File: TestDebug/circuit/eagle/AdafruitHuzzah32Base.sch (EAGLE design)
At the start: 5 parts, among them J1 CORTEX_DEBUG_PTH

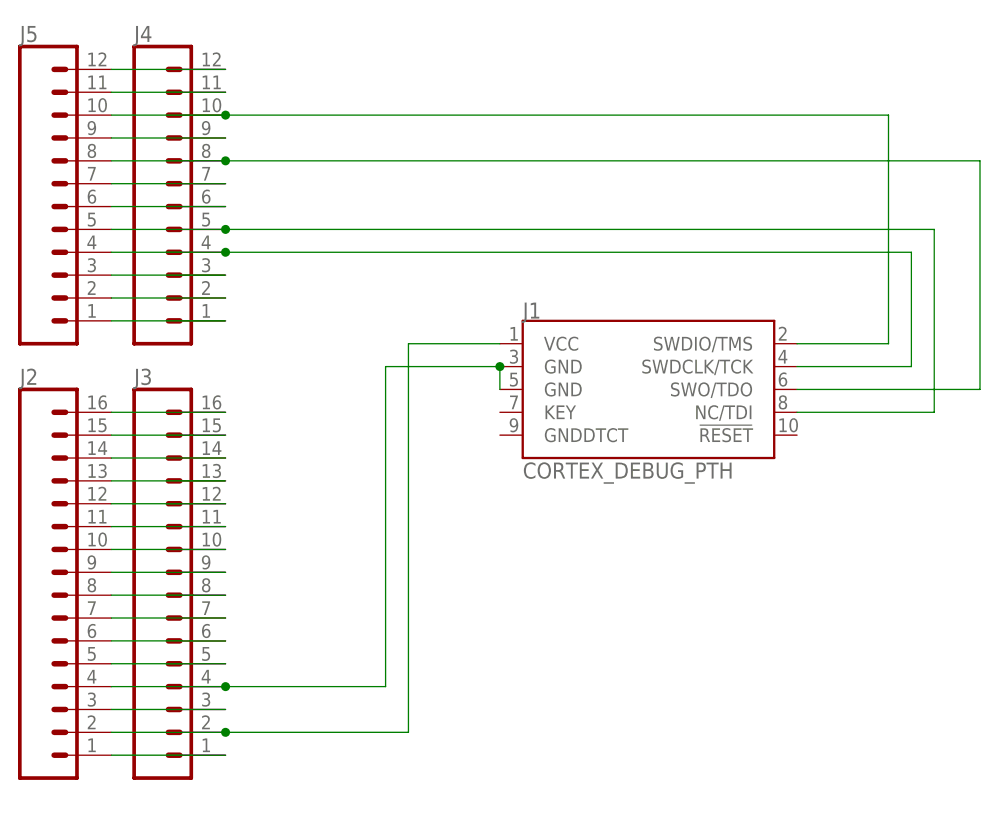
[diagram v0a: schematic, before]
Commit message: Added power pins and more silk screen
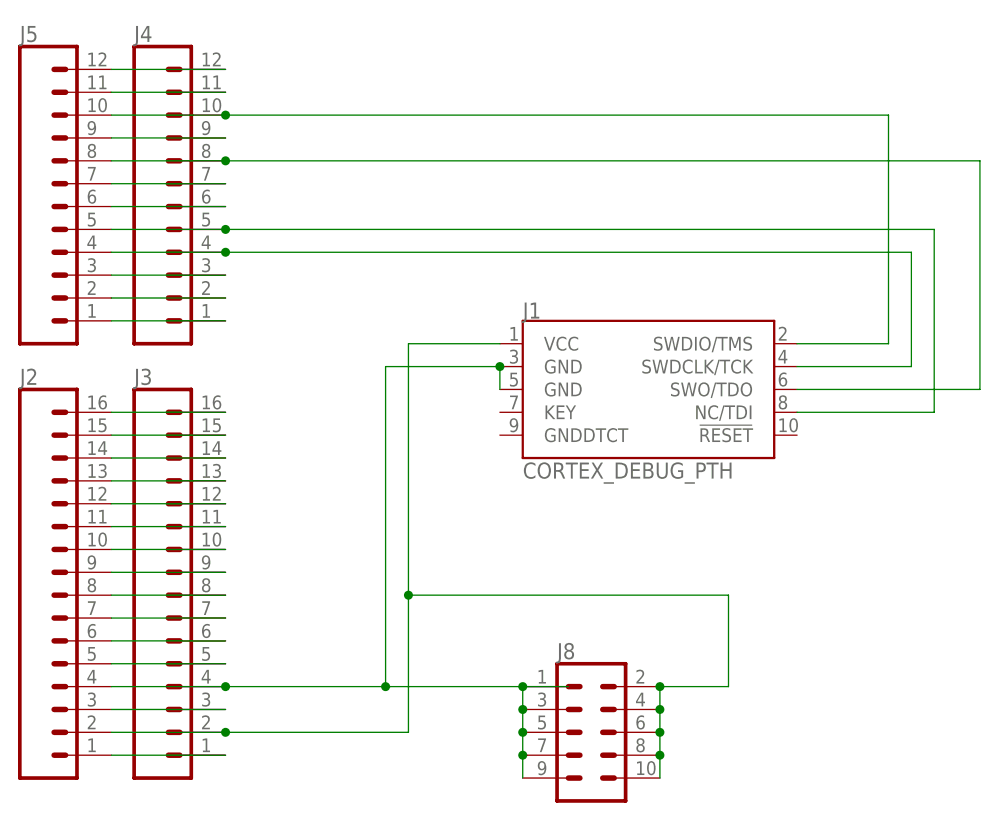
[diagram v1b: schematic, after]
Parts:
- added J8: (no value), SparkFun-Connectors:CONN_05X2PTH
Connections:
- net N$1: now also J8.10, J8.2, J8.4, J8.6, J8.8
- net N$2: now also J8.1, J8.3, J8.5, J8.7, J8.9
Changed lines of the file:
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@@
 <part name="J2" library="SparkFun-Connectors" library_urn="urn:adsk.eagle:library:513" deviceset="CONN_16" device="" package3d_urn="urn:adsk.eagle:package:38258/1"/>
 <part name="J5" library="SparkFun-Connectors" library_urn="urn:adsk.eagle:library:513" deviceset="CONN_12" device="" package3d_urn="urn:adsk.eagle:package:38169/1"/>
+<part name="J8" library="SparkFun-Connectors" library_urn="urn:adsk.eagle:library:513" deviceset="CONN_05X2" device="PTH" package3d_urn="urn:adsk.eagle:package:38012/1"/>
 </parts>
 <sheets>
@@
 <attribute name="NAME" x="50.8" y="104.648" size="1.778" layer="95" font="vector"/>
 </instance>
+<instance part="J8" gate="G$1" x="114.3" y="27.94" smashed="yes">
+<attribute name="VALUE" x="110.49" y="18.034" size="1.778" layer="96" font="vector"/>
+<attribute name="NAME" x="110.49" y="36.068" size="1.778" layer="95" font="vector"/>
+</instance>
 </instances>
 <busses>
@@
 <pinref part="J3" gate="G$1" pin="2"/>
 <wire x1="73.66" y1="27.94" x2="93.98" y2="27.94" width="0.1524" layer="91"/>
-<wire x1="93.98" y1="27.94" x2="93.98" y2="71.12" width="0.1524" layer="91"/>
+<wire x1="93.98" y1="27.94" x2="93.98" y2="43.18" width="0.1524" layer="91"/>
 <pinref part="J1" gate="G$1" pin="VCC"/>
+<wire x1="93.98" y1="43.18" x2="93.98" y2="71.12" width="0.1524" layer="91"/>
 <wire x1="93.98" y1="71.12" x2="104.14" y2="71.12" width="0.1524" layer="91"/>
 <pinref part="J2" gate="G$1" pin="2"/>
 <wire x1="60.96" y1="27.94" x2="73.66" y2="27.94" width="0.1524" layer="91"/>
 <junction x="73.66" y="27.94"/>
+<wire x1="93.98" y1="43.18" x2="129.54" y2="43.18" width="0.1524" layer="91"/>
+<wire x1="129.54" y1="43.18" x2="129.54" y2="33.02" width="0.1524" layer="91"/>
+<junction x="93.98" y="43.18"/>
+<pinref part="J8" gate="G$1" pin="2"/>
+<wire x1="129.54" y1="33.02" x2="121.92" y2="33.02" width="0.1524" layer="91"/>
+<pinref part="J8" gate="G$1" pin="4"/>
+<wire x1="121.92" y1="30.48" x2="121.92" y2="33.02" width="0.1524" layer="91"/>
+<junction x="121.92" y="33.02"/>
+<pinref part="J8" gate="G$1" pin="6"/>
+<wire x1="121.92" y1="27.94" x2="121.92" y2="30.48" width="0.1524" layer="91"/>
+<junction x="121.92" y="30.48"/>
+<pinref part="J8" gate="G$1" pin="8"/>
+<wire x1="121.92" y1="25.4" x2="121.92" y2="27.94" width="0.1524" layer="91"/>
+<junction x="121.92" y="27.94"/>
+<pinref part="J8" gate="G$1" pin="10"/>
+<wire x1="121.92" y1="22.86" x2="121.92" y2="25.4" width="0.1524" layer="91"/>
+<junction x="121.92" y="25.4"/>
 </segment>
 </net>
@@
 <wire x1="60.96" y1="33.02" x2="73.66" y2="33.02" width="0.1524" layer="91"/>
 <junction x="73.66" y="33.02"/>
+<wire x1="91.44" y1="33.02" x2="106.68" y2="33.02" width="0.1524" layer="91"/>
+<junction x="91.44" y="33.02"/>
+<pinref part="J8" gate="G$1" pin="1"/>
+<wire x1="106.68" y1="33.02" x2="111.76" y2="33.02" width="0.1524" layer="91"/>
+<junction x="106.68" y="33.02"/>
+<pinref part="J8" gate="G$1" pin="3"/>
+<wire x1="106.68" y1="33.02" x2="106.68" y2="30.48" width="0.1524" layer="91"/>
+<pinref part="J8" gate="G$1" pin="5"/>
+<wire x1="106.68" y1="27.94" x2="106.68" y2="30.48" width="0.1524" layer="91"/>
+<junction x="106.68" y="30.48"/>
+<pinref part="J8" gate="G$1" pin="7"/>
+<wire x1="106.68" y1="25.4" x2="106.68" y2="27.94" width="0.1524" layer="91"/>
+<junction x="106.68" y="27.94"/>
+<pinref part="J8" gate="G$1" pin="9"/>
+<wire x1="106.68" y1="22.86" x2="106.68" y2="25.4" width="0.1524" layer="91"/>
+<junction x="106.68" y="25.4"/>
 </segment>
 </net>
